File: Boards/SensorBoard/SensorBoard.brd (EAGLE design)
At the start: 36.4 x 54.8 mm, 14 parts

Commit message: Revised sensor board
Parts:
- moved U$3 35.2 mm to (19.1, 45.8), flipped to the bottom
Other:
- board size 36.4 x 54.8 mm -> 34.2 x 52.6 mm
- board text added: "(c) Pioneers In Engineering Design by: Seiya O, Averal K, Margo O, Steven L This design is open source hardware. For more information, visit pioneers.berkeley.edu/opensource"
- board text added: "SensorBoard Rev A"
- board text removed: "(c) Pioneers In Engineering Design by: Seiya O, Averal K, Margo O This design is open source hardware. For more information, visit pioneers.berkeley.edu/opensource"
- board text removed: "+"
- board text removed: "10k"
- board text removed: "330"
- board text removed: "TwistIt! Prod"
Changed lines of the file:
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@@
 <layer number="20" name="Dimension" color="15" fill="1" visible="yes" active="yes"/>
 <layer number="21" name="tPlace" color="15" fill="1" visible="yes" active="yes"/>
-<layer number="22" name="bPlace" color="15" fill="1" visible="no" active="yes"/>
+<layer number="22" name="bPlace" color="15" fill="1" visible="yes" active="yes"/>
 <layer number="23" name="tOrigins" color="15" fill="1" visible="yes" active="yes"/>
-<layer number="24" name="bOrigins" color="15" fill="1" visible="no" active="yes"/>
+<layer number="24" name="bOrigins" color="15" fill="1" visible="yes" active="yes"/>
 <layer number="25" name="tNames" color="7" fill="1" visible="yes" active="yes"/>
-<layer number="26" name="bNames" color="7" fill="1" visible="no" active="yes"/>
-<layer number="27" name="tValues" color="7" fill="1" visible="no" active="yes"/>
-<layer number="28" name="bValues" color="7" fill="1" visible="no" active="yes"/>
+<layer number="26" name="bNames" color="7" fill="1" visible="yes" active="yes"/>
+<layer number="27" name="tValues" color="7" fill="1" visible="yes" active="yes"/>
+<layer number="28" name="bValues" color="7" fill="1" visible="yes" active="yes"/>
 <layer number="29" name="tStop" color="7" fill="3" visible="no" active="yes"/>
 <layer number="30" name="bStop" color="7" fill="6" visible="no" active="yes"/>
@@
 <board>
 <plain>
-<wire x1="0" y1="0" x2="36.4" y2="0" width="0" layer="20"/>
-<wire x1="36.4" y1="0" x2="36.4" y2="54.788" width="0" layer="20"/>
-<wire x1="36.4" y1="54.788" x2="0" y2="54.788" width="0" layer="20"/>
-<wire x1="0" y1="54.788" x2="0" y2="0" width="0" layer="20"/>
+<wire x1="2.159" y1="2.286" x2="36.4" y2="2.286" width="0" layer="20"/>
+<wire x1="36.4" y1="2.286" x2="36.4" y2="54.788" width="0" layer="20"/>
+<wire x1="36.4" y1="54.788" x2="2.159" y2="54.8642" width="0" layer="20"/>
+<wire x1="2.159" y1="54.8642" x2="2.159" y2="2.286" width="0" layer="20"/>
 <text x="24.638" y="10.922" size="0.99" layer="26" font="vector" rot="MR90" align="top-left">(c) Pioneers In Engineering
-Design by: Seiya O, Averal K, Margo O
+Design by: Seiya O, Averal K,
+          Margo O, Steven L
 This design is open source hardware.
 For more information, visit
 pioneers.berkeley.edu/opensource</text>
-<text x="19.63" y="50.53" size="1.778" layer="21" font="vector" ratio="15" align="center">TwistIt!
-Prod</text>
-<text x="29.483" y="37.492" size="0.8128" layer="25" font="vector">Pull-up
+<text x="19.63" y="50.53" size="1.778" layer="21" font="vector" ratio="15" align="center">SensorBoard
+Rev A</text>
+<text x="30.0926" y="36.3998" size="0.8128" layer="25" font="vector">Pull-up
 Jumper</text>
-<text x="8.067" y="32.024" size="0.8128" layer="26" rot="MR270">TwistIt: A Mulitpurpose board
+<text x="9.21" y="40.3298" size="0.8128" layer="26" font="vector" rot="MR270">TwistIt: A Mulitpurpose board
 that takes line following array,
 potentiometers, limit switches,
 reed switches, and the Yogi
 Bear Motor Controller Board.</text>
-<text x="10.025" y="27.64" size="0.8128" layer="25" font="vector" rot="MR0">+</text>
-<text x="10.058" y="24.313" size="0.8128" layer="25" font="vector" rot="MR0">+</text>
-<text x="10.003" y="20.986" size="0.8128" layer="25" font="vector" rot="MR0">+</text>
-<text x="33.7566" y="29.2862" size="0.4064" layer="21" font="vector" rot="R90">10k</text>
-<text x="33.8074" y="24.5364" size="0.4064" layer="21" font="vector" rot="R90">330</text>
 </plain>
 <attributes>
@@
 <attribute name="REFERENCE_DEST" value="ARDUINO_PRO_MICRO" x="10.16" y="11.43" size="1.778" layer="27" display="off"/>
 </element>
-<element name="U$3" library="pie" package="PIE-LOGO-SMALL" value="" x="5.197" y="13.538"/>
+<element name="U$3" library="pie" package="PIE-LOGO-SMALL" value="" x="19.1162" y="45.8468" rot="MR0"/>
 <element name="U$4" library="pie" package="OSHW-LOGO-S" value="" x="33.99" y="16.095" rot="MR0"/>
 <element name="U$1" library="pie" package="STAND-OFF" value="" x="32.004" y="50.8"/>
@@
 <element name="SJ1" library="pie" package="SJ_2S-NO" value="SOLDERJUMPERNO" x="32.0548" y="34.3154" smashed="yes" rot="R270">
 <attribute name="PIE-INT-REF-NUM" value="DNL" x="32.0548" y="34.3154" size="1.778" layer="27" rot="R270" display="off"/>
-<attribute name="VALUE" x="29.5148" y="35.5854" size="1.27" layer="27" font="vector" rot="R270"/>
 </element>
 <element name="R1" library="pie" package="4X-0603" value="10k" x="31.2928" y="31.0134" smashed="yes" rot="R270">
@@
 <contactref element="APM" pad="GND@0"/>
 <polygon width="0.4064" layer="16">
-<vertex x="0" y="54.61"/>
+<vertex x="1.8542" y="54.61"/>
 <vertex x="36.3" y="54.61"/>
-<vertex x="36.3" y="0"/>
-<vertex x="0" y="0"/>
+<vertex x="36.3" y="2.1844"/>
+<vertex x="1.8542" y="2.1844"/>
 </polygon>
 <contactref element="APM" pad="GND@1"/>

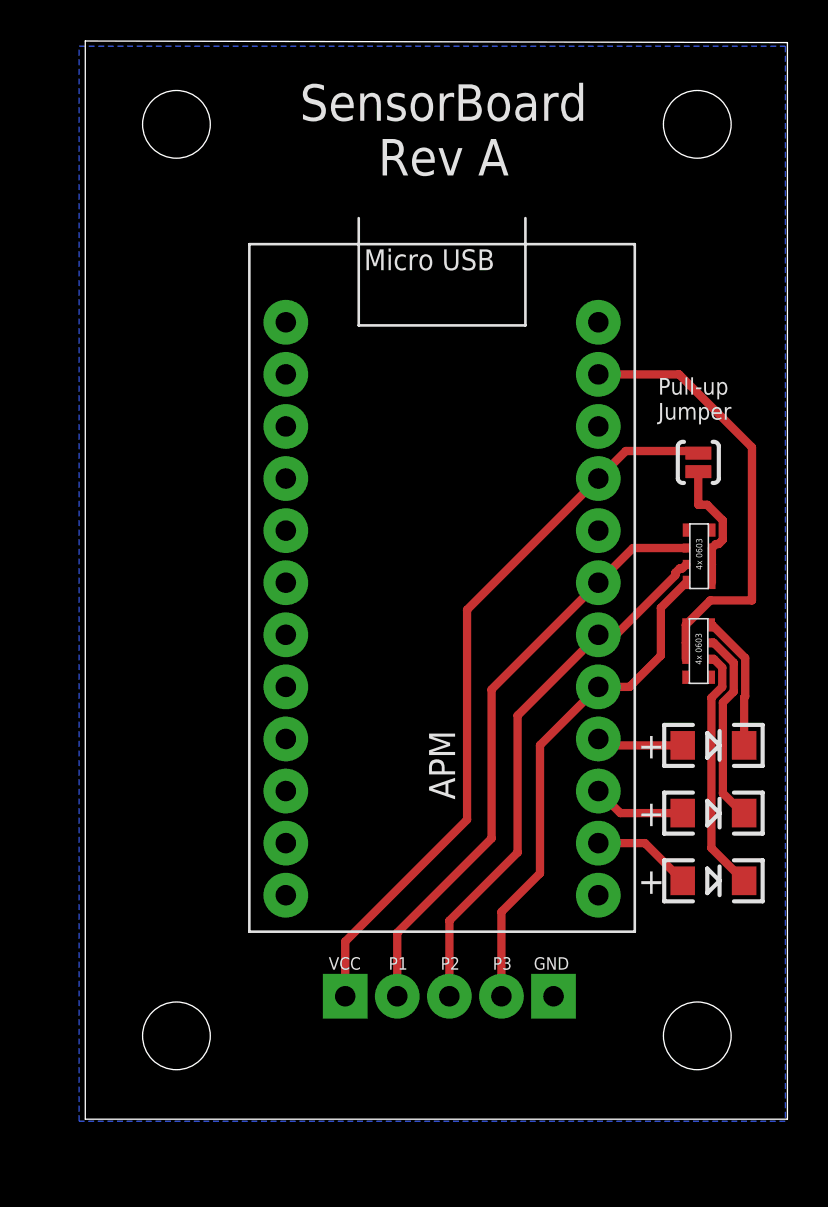
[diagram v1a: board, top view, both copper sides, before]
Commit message: Revised SensorBoard and fixed TwistIt
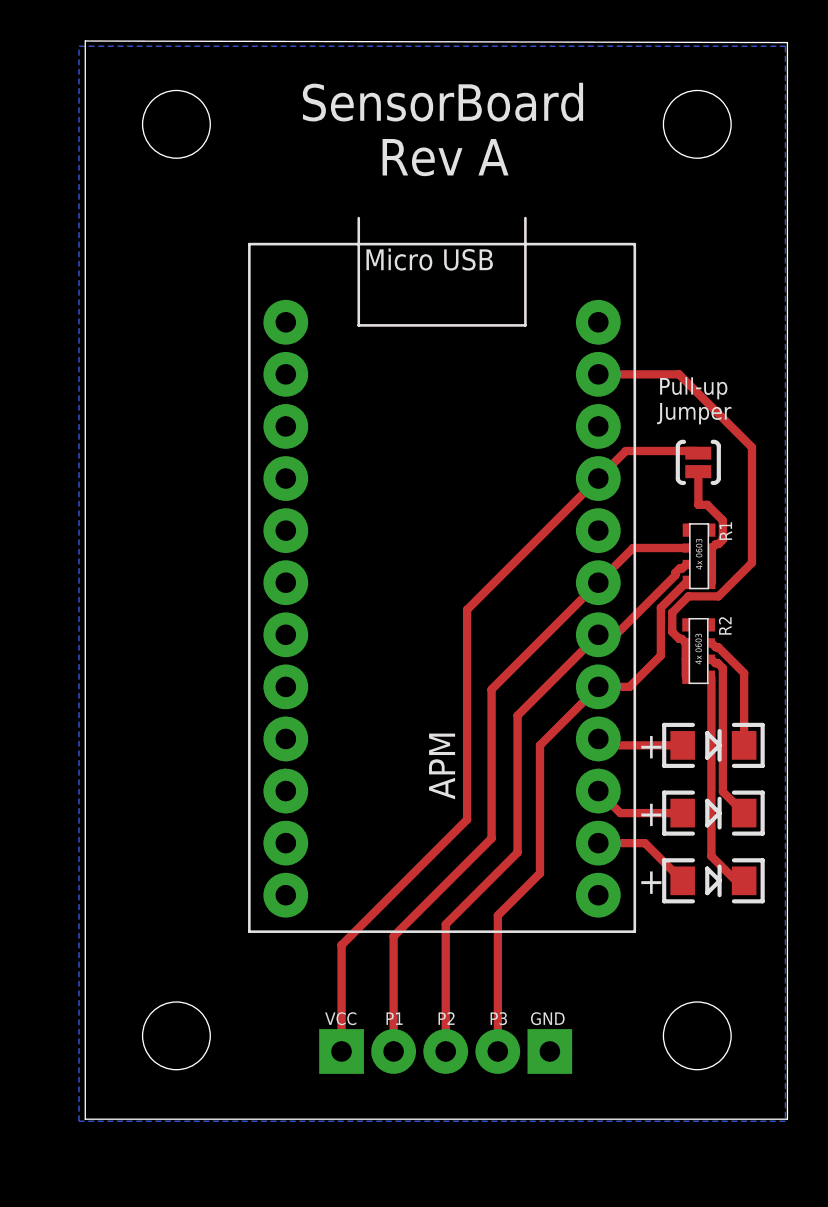
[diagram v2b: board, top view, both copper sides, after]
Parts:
- moved U$2 2.70 mm to (24.8, 5.59)
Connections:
- removed net N$4: LED2.C, R2.7
- new net N$1: LED2.C, R2.6
- net GND: now also R2.4; no longer R2.1
- net N$2: now also R2.5; no longer R2.6
- net N$6: now also R2.7; no longer R2.8
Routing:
- net N$4: track 9.52 -> 0.00 mm
- net N$1: track 0.00 -> 8.24 mm
- net P3: track 24.8 -> 27.6 mm
- net VCC: track 35.8 -> 38.6 mm
- net P2: track 26.4 -> 29.2 mm
- net P1: track 29.2 -> 32.0 mm
- net N$2: track 12.1 -> 10.8 mm
- net GND: track 21.8 -> 23.0 mm
- net N$6: track 6.67 -> 5.73 mm
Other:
- board text added: "SensorBoard: A multipurpose board that takes line following array and limit switches"
- board text removed: "TwistIt: A Mulitpurpose board that takes line following array, potentiometers, limit switches, reed switches, and the Yogi Bear Motor Controller Board."
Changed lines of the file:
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@@
 <text x="30.0926" y="36.3998" size="0.8128" layer="25" font="vector">Pull-up
 Jumper</text>
-<text x="9.21" y="40.3298" size="0.8128" layer="26" font="vector" rot="MR270">TwistIt: A Mulitpurpose board
-that takes line following array,
-potentiometers, limit switches,
-reed switches, and the Yogi
-Bear Motor Controller Board.</text>
+<text x="9.21" y="40.3298" size="0.8128" layer="26" font="vector" rot="MR270">SensorBoard: A multipurpose board
+that takes line following array
+and limit switches</text>
 </plain>
 <attributes>
@@
 <attribute name="VALUE" x="34.1876" y="19.2442" size="0.762" layer="27" font="vector" rot="R180"/>
 </element>
-<element name="U$2" library="pie" package="5PIN" value="5PIN" x="24.9936" y="8.2804" smashed="yes" rot="R180"/>
+<element name="U$2" library="pie" package="5PIN" value="5PIN" x="24.8158" y="5.588" smashed="yes" rot="R180"/>
 <element name="SJ1" library="pie" package="SJ_2S-NO" value="SOLDERJUMPERNO" x="32.0548" y="34.3154" smashed="yes" rot="R270">
 <attribute name="PIE-INT-REF-NUM" value="DNL" x="32.0548" y="34.3154" size="1.778" layer="27" rot="R270" display="off"/>
 </element>
-<element name="R1" library="pie" package="4X-0603" value="10k" x="31.2928" y="31.0134" smashed="yes" rot="R270">
-<attribute name="VALUE" x="30.5428" y="31.4134" size="0.6096" layer="27" font="vector" rot="R270"/>
-</element>
-<element name="R2" library="pie" package="4X-0603" value="330" x="31.2674" y="26.3906" smashed="yes" rot="R270">
-<attribute name="VALUE" x="30.5174" y="26.7906" size="0.6096" layer="27" font="vector" rot="R270"/>
-</element>
+<element name="R1" library="pie" package="4X-0603" value="10k" x="31.2928" y="31.0134" rot="R270"/>
+<element name="R2" library="pie" package="4X-0603" value="330" x="31.2674" y="26.3906" rot="R270"/>
 <element name="U$7" library="pie" package="STAND-OFF" value="" x="32.004" y="6.35"/>
 </elements>
@@
 <contactref element="APM" pad="GND@2"/>
 <contactref element="U$2" pad="GND"/>
-<contactref element="R2" pad="1"/>
 <contactref element="R2" pad="2"/>
 <contactref element="R2" pad="3"/>
 <wire x1="31.4424" y1="24.7156" x2="31.4424" y2="25.5156" width="0.4064" layer="1"/>
-<wire x1="31.4424" y1="25.5156" x2="31.4424" y2="26.3906" width="0.4064" layer="1"/>
-<wire x1="31.4424" y1="26.3906" x2="32.6362" y2="27.5844" width="0.4064" layer="1"/>
-<wire x1="32.6362" y1="27.5844" x2="34.671" y2="27.5844" width="0.4064" layer="1"/>
-<wire x1="34.671" y1="27.5844" x2="34.671" y2="35.052" width="0.4064" layer="1"/>
 <wire x1="31.115" y1="38.608" x2="27.178" y2="38.608" width="0.4064" layer="1"/>
 <wire x1="34.671" y1="35.052" x2="31.115" y2="38.608" width="0.4064" layer="1"/>
+<wire x1="34.671" y1="29.41370625" x2="33.04009375" y2="27.7828" width="0.4064" layer="1"/>
+<wire x1="34.671" y1="29.41370625" x2="34.671" y2="35.052" width="0.4064" layer="1"/>
+<contactref element="R2" pad="4"/>
+<wire x1="31.57746875" y1="27.7828" x2="30.7848" y2="26.99013125" width="0.4064" layer="1"/>
+<wire x1="31.12010625" y1="25.71" x2="31.248" y2="25.71" width="0.4064" layer="1"/>
+<wire x1="31.248" y1="25.71" x2="31.4424" y2="25.5156" width="0.4064" layer="1"/>
+<wire x1="30.7848" y1="26.99013125" x2="30.7848" y2="26.04530625" width="0.4064" layer="1"/>
+<wire x1="30.7848" y1="26.04530625" x2="31.12010625" y2="25.71" width="0.4064" layer="1"/>
+<wire x1="33.04009375" y1="27.7828" x2="31.57746875" y2="27.7828" width="0.4064" layer="1"/>
+<wire x1="31.4424" y1="24.7156" x2="31.4424" y2="23.8406" width="0.4064" layer="1"/>
 </signal>
 <signal name="VCC">
@@
 <wire x1="27.178" y1="33.528" x2="20.7772" y2="27.1272" width="0.4064" layer="1"/>
 <wire x1="20.7772" y1="27.1272" x2="20.7772" y2="16.891" width="0.4064" layer="1"/>
-<wire x1="20.7772" y1="16.891" x2="14.8336" y2="10.9474" width="0.4064" layer="1"/>
-<wire x1="14.8336" y1="10.9474" x2="14.8336" y2="8.2804" width="0.4064" layer="1"/>
+<wire x1="20.7772" y1="16.891" x2="14.6558" y2="10.7696" width="0.4064" layer="1"/>
+<wire x1="14.6558" y1="10.7696" x2="14.6558" y2="5.588" width="0.4064" layer="1"/>
 </signal>
 <signal name="P1">
@@
 <wire x1="27.178" y1="28.448" x2="21.971" y2="23.241" width="0.4064" layer="1"/>
 <wire x1="21.971" y1="23.241" x2="21.971" y2="15.9766" width="0.4064" layer="1"/>
-<wire x1="21.971" y1="15.9766" x2="17.3736" y2="11.3792" width="0.4064" layer="1"/>
-<wire x1="17.3736" y1="11.3792" x2="17.3736" y2="8.2804" width="0.4064" layer="1"/>
+<wire x1="21.971" y1="15.9766" x2="17.1958" y2="11.2014" width="0.4064" layer="1"/>
+<wire x1="17.1958" y1="11.2014" x2="17.1958" y2="5.588" width="0.4064" layer="1"/>
 </signal>
 <signal name="P2">
@@
 <wire x1="27.178" y1="25.908" x2="23.241" y2="21.971" width="0.4064" layer="1"/>
 <wire x1="23.241" y1="21.971" x2="23.241" y2="15.2908" width="0.4064" layer="1"/>
-<wire x1="23.241" y1="15.2908" x2="19.9136" y2="11.9634" width="0.4064" layer="1"/>
-<wire x1="19.9136" y1="11.9634" x2="19.9136" y2="8.2804" width="0.4064" layer="1"/>
+<wire x1="23.241" y1="15.2908" x2="19.7358" y2="11.7856" width="0.4064" layer="1"/>
+<wire x1="19.7358" y1="11.7856" x2="19.7358" y2="5.588" width="0.4064" layer="1"/>
 </signal>
 <signal name="P3">
@@
 <wire x1="27.178" y1="23.368" x2="24.3332" y2="20.5232" width="0.4064" layer="1"/>
 <wire x1="24.3332" y1="20.5232" x2="24.3332" y2="14.2748" width="0.4064" layer="1"/>
-<wire x1="24.3332" y1="14.2748" x2="22.4536" y2="12.3952" width="0.4064" layer="1"/>
-<wire x1="22.4536" y1="12.3952" x2="22.4536" y2="8.2804" width="0.4064" layer="1"/>
+<wire x1="24.3332" y1="14.2748" x2="22.2758" y2="12.2174" width="0.4064" layer="1"/>
+<wire x1="22.2758" y1="12.2174" x2="22.2758" y2="5.588" width="0.4064" layer="1"/>
 </signal>
 <signal name="LED1">
@@
 <signal name="N$2">
 <contactref element="LED1" pad="C"/>
-<wire x1="34.2156" y1="13.9132" x2="34.2906" y2="13.9102" width="0.4064" layer="1"/>
-<contactref element="R2" pad="6"/>
-<wire x1="32.6924" y1="15.5084" x2="34.2906" y2="13.9102" width="0.4064" layer="1"/>
-<wire x1="33.223" y1="23.36830625" x2="33.223" y2="24.31289375" width="0.4064" layer="1"/>
-<wire x1="32.6924" y1="22.83770625" x2="32.6924" y2="15.5084" width="0.4064" layer="1"/>
-<wire x1="33.223" y1="23.36830625" x2="32.6924" y2="22.83770625" width="0.4064" layer="1"/>
-<wire x1="32.82029375" y1="24.7156" x2="32.6924" y2="24.7156" width="0.4064" layer="1"/>
-<wire x1="33.223" y1="24.31289375" x2="32.82029375" y2="24.7156" width="0.4064" layer="1"/>
-</signal>
-<signal name="N$4">
-<contactref element="LED2" pad="C"/>
-<wire x1="34.2156" y1="17.2152" x2="34.2906" y2="17.2122" width="0.4064" layer="1"/>
-<contactref element="R2" pad="7"/>
-<wire x1="33.2512" y1="22.6062375" x2="33.2512" y2="18.1796" width="0.4064" layer="1"/>
-<wire x1="33.2512" y1="18.1796" x2="34.2156" y2="17.2152" width="0.4064" layer="1"/>
-<wire x1="33.7818" y1="23.1368375" x2="33.7818" y2="24.5443625" width="0.4064" layer="1"/>
-<wire x1="33.7818" y1="23.1368375" x2="33.2512" y2="22.6062375" width="0.4064" layer="1"/>
-<wire x1="32.8105625" y1="25.5156" x2="32.6924" y2="25.5156" width="0.4064" layer="1"/>
-<wire x1="33.7818" y1="24.5443625" x2="32.8105625" y2="25.5156" width="0.4064" layer="1"/>
+<wire x1="33.8926" y1="13.9102" x2="34.2906" y2="13.9102" width="0.4064" layer="1"/>
+<contactref element="R2" pad="5"/>
+<wire x1="32.6924" y1="23.8406" x2="32.6924" y2="15.1104" width="0.4064" layer="1"/>
+<wire x1="32.6924" y1="15.1104" x2="33.8926" y2="13.9102" width="0.4064" layer="1"/>
 </signal>
 <signal name="N$6">
 <contactref element="LED3" pad="C"/>
-<wire x1="34.2156" y1="20.5172" x2="34.2906" y2="20.5142" width="0.4064" layer="1"/>
-<contactref element="R2" pad="8"/>
-<wire x1="34.3406" y1="22.90536875" x2="34.2906" y2="22.85536875" width="0.4064" layer="1"/>
-<wire x1="34.2906" y1="22.85536875" x2="34.2906" y2="20.5142" width="0.4064" layer="1"/>
-<wire x1="34.3406" y1="22.90536875" x2="34.3406" y2="24.77583125" width="0.4064" layer="1"/>
-<wire x1="32.72583125" y1="26.3906" x2="32.6924" y2="26.3906" width="0.4064" layer="1"/>
-<wire x1="34.3406" y1="24.77583125" x2="32.72583125" y2="26.3906" width="0.4064" layer="1"/>
+<contactref element="R2" pad="7"/>
+<wire x1="32.6924" y1="25.5156" x2="32.9118" y2="25.2962" width="0.4064" layer="1"/>
+<wire x1="32.9118" y1="25.2962" x2="33.0299625" y2="25.2962" width="0.4064" layer="1"/>
+<wire x1="33.0299625" y1="25.2962" x2="34.2906" y2="24.0355625" width="0.4064" layer="1"/>
+<wire x1="34.2906" y1="24.0355625" x2="34.2906" y2="20.5142" width="0.4064" layer="1"/>
+</signal>
+<signal name="N$1">
+<contactref element="LED2" pad="C"/>
+<contactref element="R2" pad="6"/>
+<wire x1="33.2512" y1="18.2516" x2="34.2906" y2="17.2122" width="0.4064" layer="1"/>
+<wire x1="33.2512" y1="24.28469375" x2="33.2512" y2="18.2516" width="0.4064" layer="1"/>
+<wire x1="32.6924" y1="24.7156" x2="32.8868" y2="24.5212" width="0.4064" layer="1"/>
+<wire x1="32.8868" y1="24.5212" x2="33.01469375" y2="24.5212" width="0.4064" layer="1"/>
+<wire x1="33.01469375" y1="24.5212" x2="33.2512" y2="24.28469375" width="0.4064" layer="1"/>
 </signal>
 </signals>
